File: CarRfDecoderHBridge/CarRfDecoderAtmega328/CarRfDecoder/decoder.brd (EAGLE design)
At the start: 98.7 x 80 mm, 55 parts, among them U2 RFM69CW, U3 MCP73831, U4 ATMEGA328P, U6 MIC5219 3.3V, Y1 16MHZ

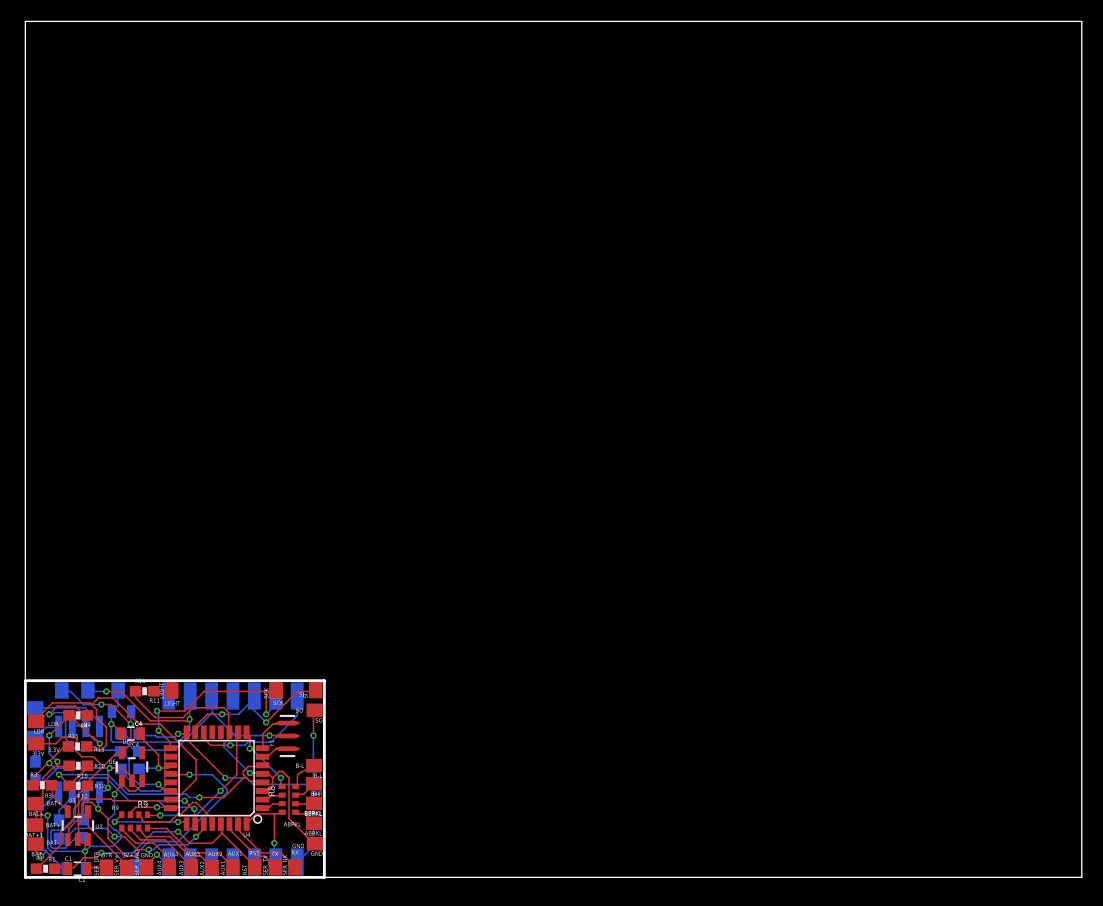
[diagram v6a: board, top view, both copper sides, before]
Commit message: Add a new version of the rc board, now smaller
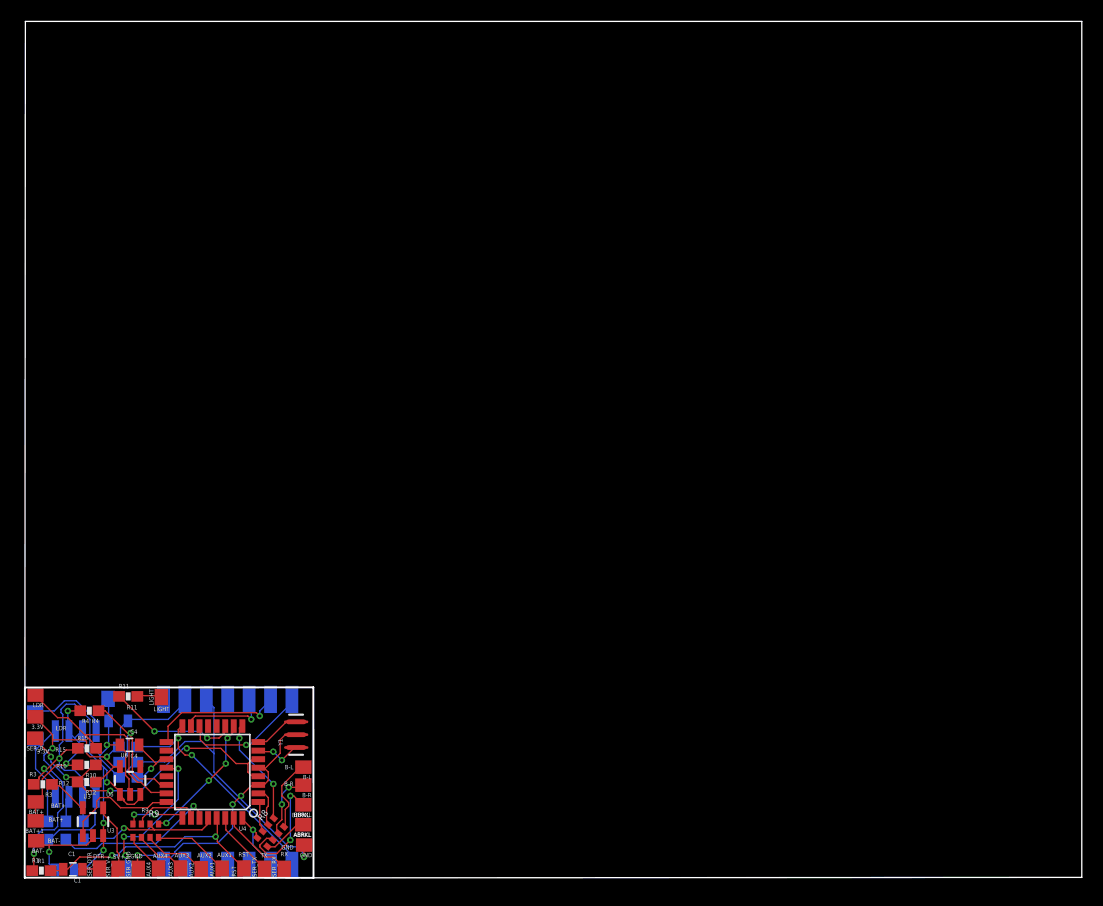
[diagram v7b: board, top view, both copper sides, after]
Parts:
- removed SCK, SI, SO, VJ, VJ1: (no value), wirepad:SMD1,27-2,54
- added SER_B: (no value), wirepad:SMD1,27-2,54
- moved R14 5.69 mm to (3.38, 4.37)
- moved R8 3.52 mm to (24.2, 4.21), turned to 230 degrees
- moved 3.3V 2.51 mm to (2.20, 15.0)
- moved LDR 2.46 mm to (2.22, 17.0)
- moved R11 1.61 mm to (10.9, 16.9)
- moved U3 1.46 mm to (7.59, 5.21)
- moved R9 1.36 mm to (12.5, 4.36)
- moved U6 1.29 mm to (11.1, 9.06)
- moved R13 1.24 mm to (10.9, 12.2)
- moved GND1 1.23 mm to (9.00, 16.7)
- moved LIGHT 1.15 mm to (14.0, 16.8)
- moved R4 1.14 mm to (7.25, 15.6)
- moved C4 1.06 mm to (11.0, 12.4)
- moved B-L 1.02 mm to (27.2, 10.3)
- moved ABRKL 1.02 mm to (27.2, 4.92)
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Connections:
- removed net N$1: R13.1, U2.2, VJ.1
- net MISO: no longer SO.1
- net MOSI: no longer SI.1
- net N$8: now also SER_B.1
- net SCK: no longer SCK.1
- net VCC: now also R13.1, U2.2; no longer VJ1.1
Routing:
- net N$1: track 21.3 -> 0.00 mm, vias 2 -> 0
- net A5: track 32.0 -> 13.7 mm
- net MISO: track 34.1 -> 22.2 mm, vias 3 -> 2
- net GND: track 104.3 -> 115.0 mm, vias 9 -> 8
- net A0: track 30.0 -> 19.7 mm
- net N$18: track 1.76 -> 11.0 mm, vias 0 -> 2
- net MOSI: track 16.7 -> 8.41 mm, vias 2 -> 1
- net BAT+: track 45.2 -> 37.1 mm, vias 6 -> 5
- net SCK: track 20.2 -> 12.8 mm, vias 3 -> 1
- net A7: track 20.8 -> 14.6 mm, vias 2 -> 1
- net OA: track 4.95 -> 10.8 mm
- net AREF: track 18.3 -> 13.6 mm, vias 1 -> 3
- net VCC: track 34.8 -> 39.4 mm, vias 2 -> 3
- net N$16: track 2.17 -> 6.35 mm, vias 0 -> 2
- net N$13: track 2.98 -> 7.07 mm
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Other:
- board size 98.7 x 80 mm -> 98.8 x 80 mm
- board text removed: "SCK"
- board text removed: "SI"
- board text removed: "SO"
